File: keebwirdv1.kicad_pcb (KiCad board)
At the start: 2 copper layers, 248.1 x 107.5 mm, 70 parts, among them SW1 SW_Push, U0 ProMicro

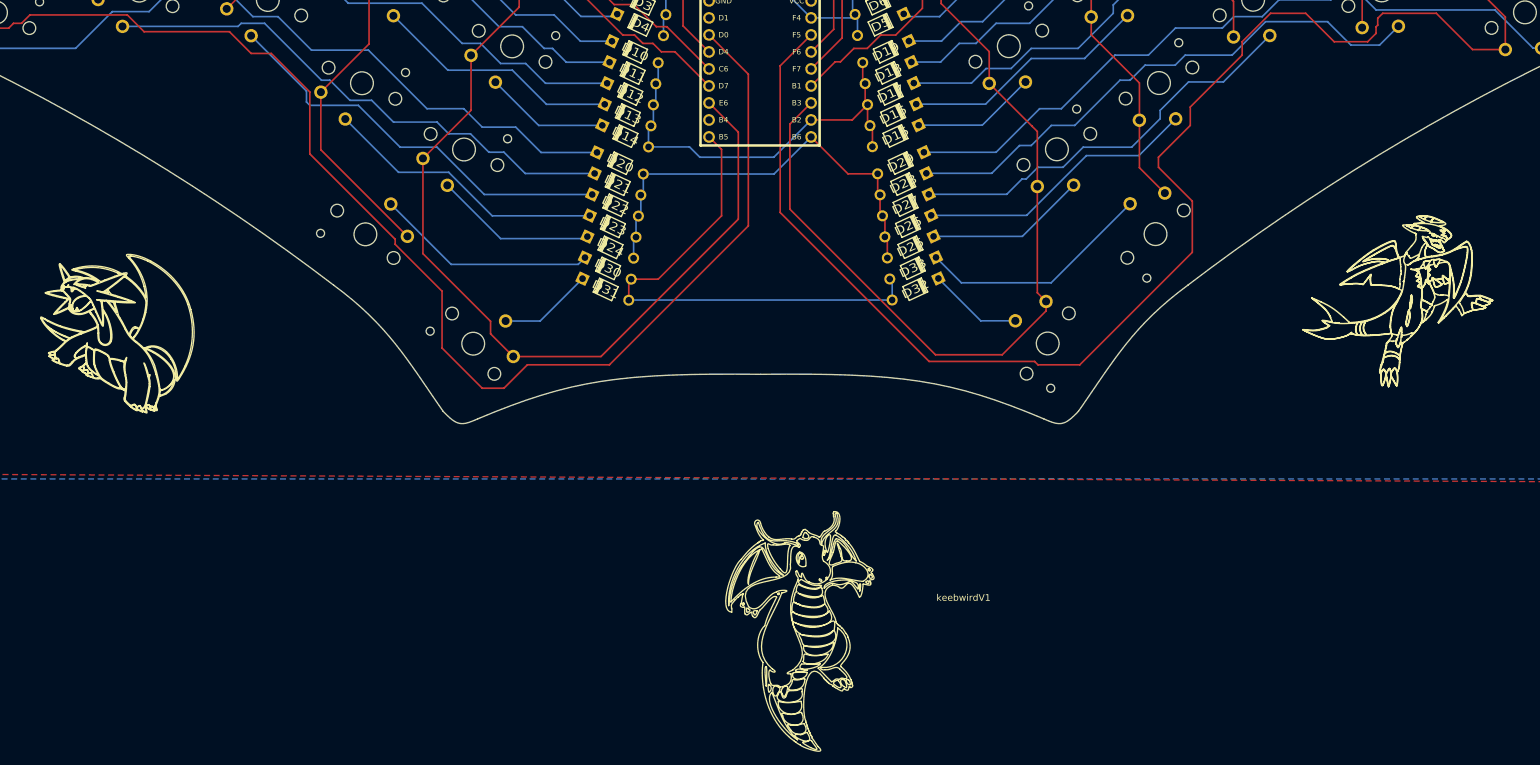
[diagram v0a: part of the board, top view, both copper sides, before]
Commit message: updated silkscreen
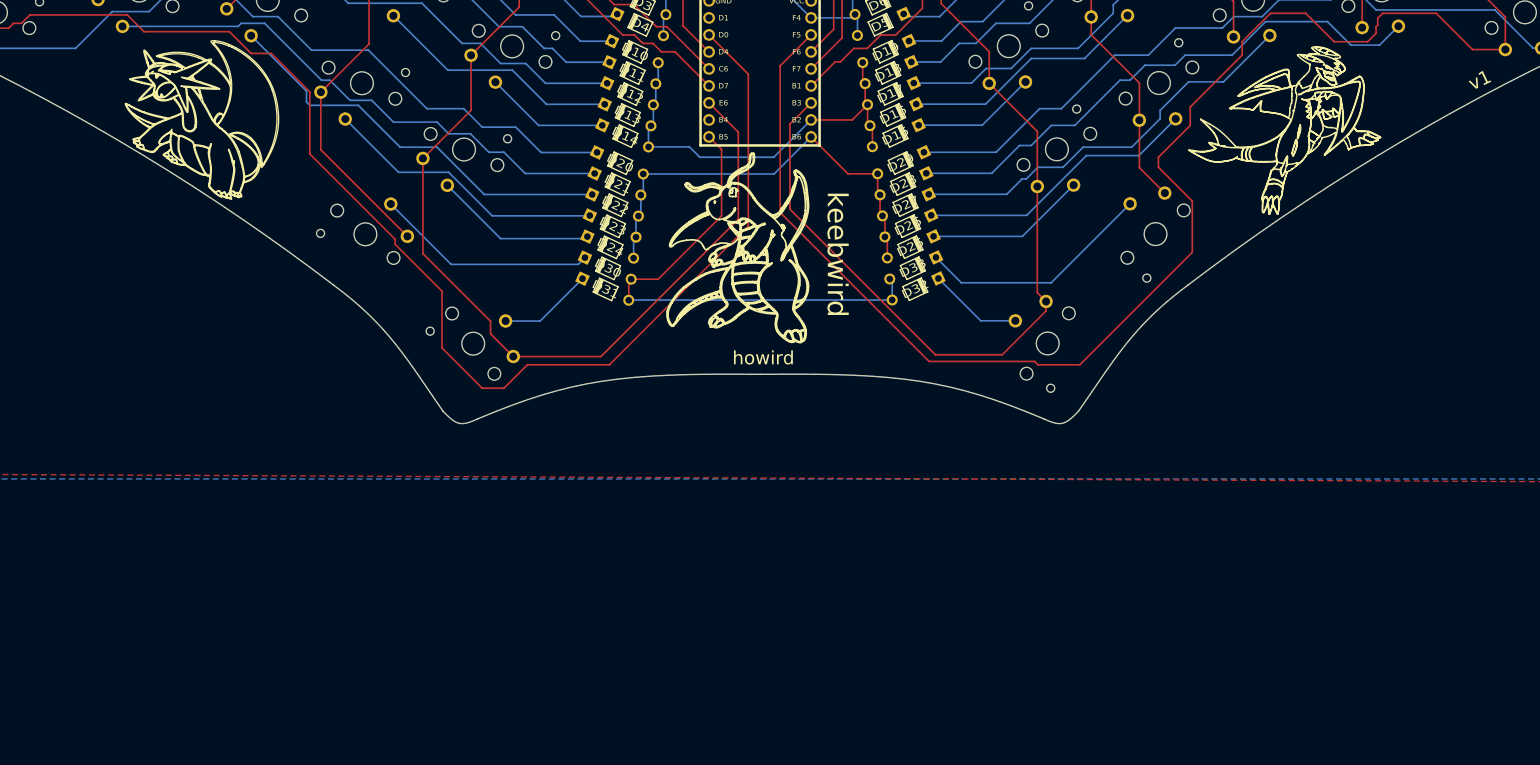
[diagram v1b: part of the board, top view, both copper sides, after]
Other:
- board text added: "howird"
- board text added: "keebwird"
- board text added: "v1"
- board text removed: "keebwirdV1"
